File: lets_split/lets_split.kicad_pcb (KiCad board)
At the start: 2 copper layers, 112 x 79 mm, 62 parts, among them J1 3PIN, J2 6PIN, J3 3PIN, SW1 SW_PUSH, SW10 SW_PUSH, SW11 SW_PUSH, SW12 SW_PUSH, SW13 SW_PUSH, SW14 SW_PUSH, SW15 SW_PUSH, SW16 SW_PUSH, SW17 SW_PUSH, SW18 SW_PUSH, SW19 SW_PUSH, SW2 SW_PUSH, SW21 SW_PUSH, SW22 SW_PUSH, SW23 SW_PUSH, SW3 SW_PUSH, SW4 SW_PUSH, SW5 SW_PUSH, SW6 SW_PUSH, SW7 SW_PUSH, SW8 SW_PUSH, SW9 SW_PUSH, U2 HOLE, U3 HOLE, U4 HOLE, U5 HOLE

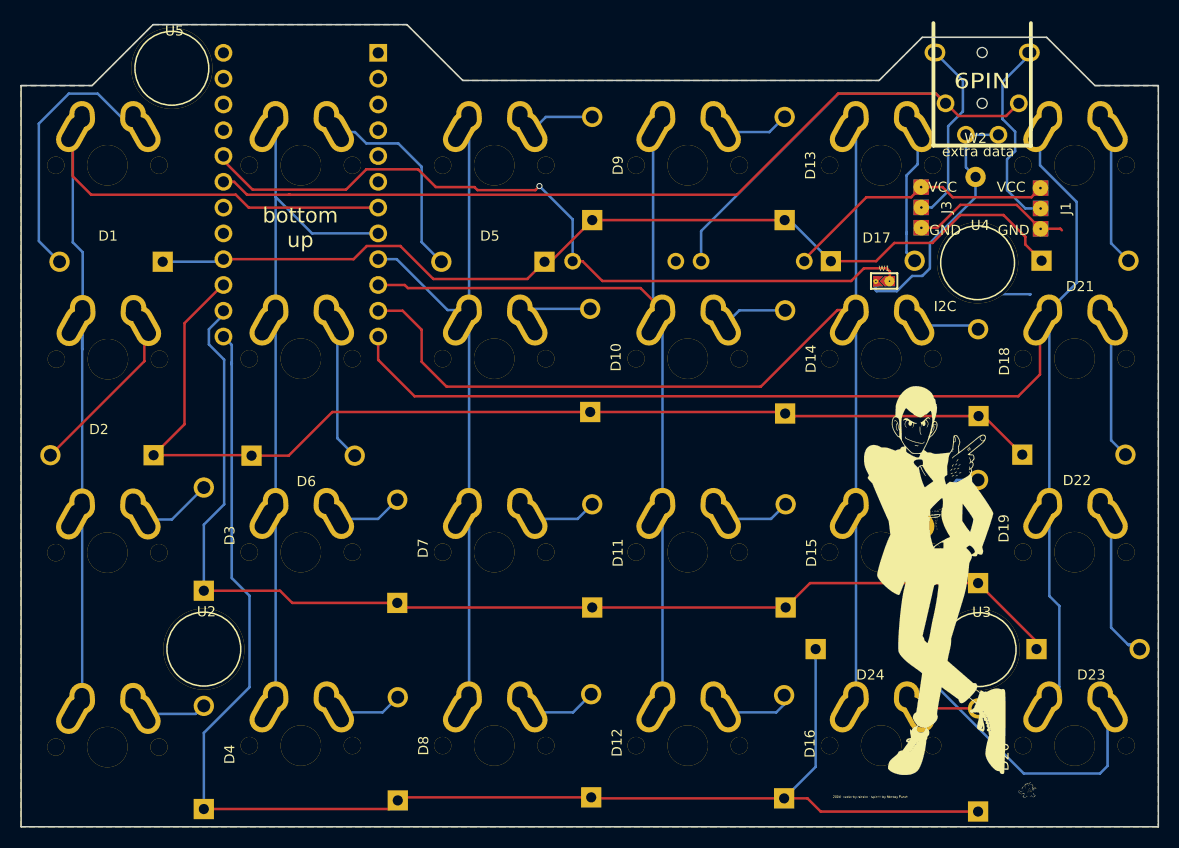
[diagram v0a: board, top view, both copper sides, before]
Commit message: Replace diode modules with SMD compatible one
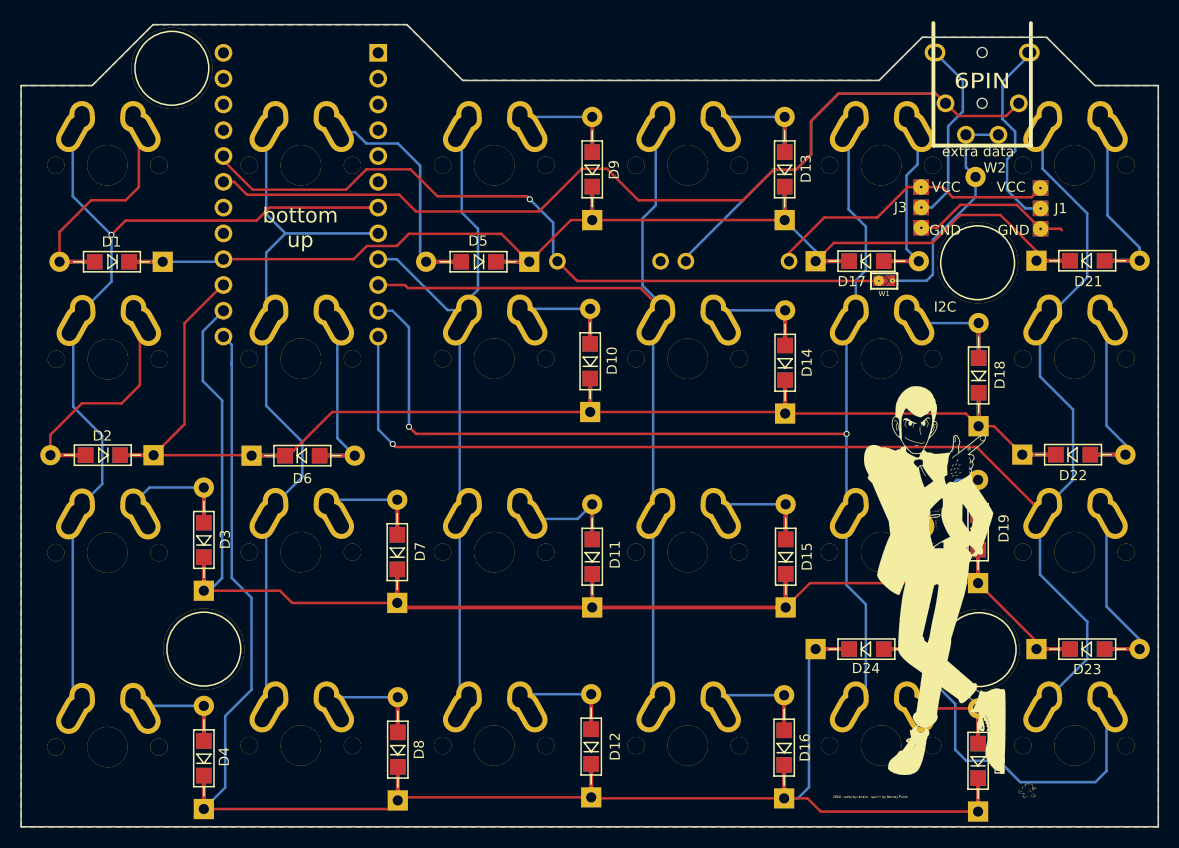
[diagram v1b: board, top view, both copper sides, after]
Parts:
- D1, D10, D11, D12, D13, D14, D15, D16, D17, D18, D19, D2, D20, D21, D22, D23, D24, D3, D4, D5, D6, D7, D8, D9: footprint Diodes_ThroughHole:Diode_DO-41_SOD81_Horizontal_RM10 -> local:Diode_TH_SOD123
- U1: value (none) -> TEENSY2.0
- moved D17 1.50 mm to (115.2, 56.3)
- moved D5 1.50 mm to (87.0, 56.4)
- moved R1 1.50 mm to (94.9, 56.3)
- moved R2 1.50 mm to (107.5, 56.3)
- moved D21 1.10 mm to (137.0, 56.2)
- moved D18 1.00 mm to (131.3, 72.5)
- turned W1 to 180 degrees
- gave numbers to parts that had none: 2
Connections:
- U1 pad 1: Net-(U1-Pad1) -> (no net)
- U1 pad 22: Net-(U1-Pad22) -> (no net)
- U1 pad 23: Net-(U1-Pad23) -> (no net)
- U1 pad 28: Net-(U1-Pad28) -> (no net)
- U1 pad 29: Net-(U1-Pad29) -> (no net)
- U1 pad 3: Net-(U1-Pad3) -> (no net)
- U1 pad 5: Net-(U1-Pad5) -> (no net)
- U1 pad 6: Net-(U1-Pad6) -> (no net)
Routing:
- net row3: track 143.1 -> 183.6 mm
- net row1: track 108.7 -> 148.7 mm
- net row2: track 117.3 -> 156.9 mm
- net row0: track 96.8 -> 136.2 mm
- net col0: track 96.5 -> 85.3 mm, vias 0 -> 1
- net Net-(D24-Pad2): track 30.5 -> 40.9 mm
- net Net-(D16-Pad2): track 7.14 -> 16.7 mm
- net Net-(D15-Pad2): track 6.65 -> 15.9 mm
- net Net-(D8-Pad2): track 6.57 -> 15.8 mm
- net Net-(D13-Pad2): track 6.57 -> 15.8 mm
- net Net-(D14-Pad2): track 6.62 -> 15.9 mm
- net Net-(D9-Pad2): track 6.67 -> 15.9 mm
- net Net-(D12-Pad2): track 6.69 -> 15.9 mm
- net Net-(D7-Pad2): track 6.69 -> 15.9 mm
- net Net-(D3-Pad2): track 7.20 -> 16.4 mm
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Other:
- net class Default: clearance 0.2 -> 0
- rule trace_clearance: 0.2 -> 0

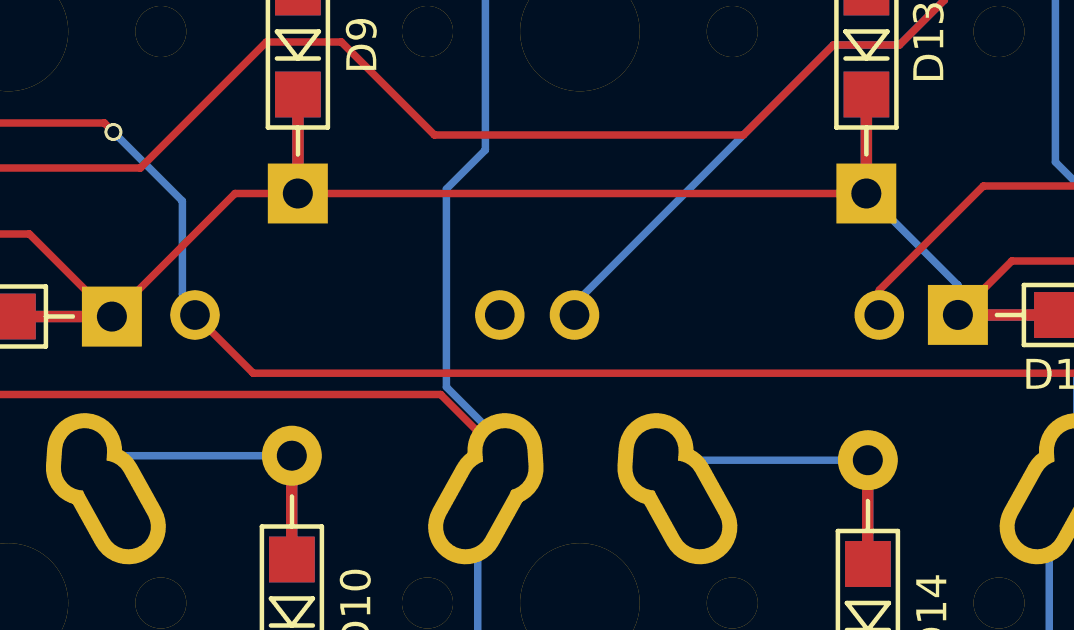
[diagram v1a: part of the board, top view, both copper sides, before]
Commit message: Replace resistor footprint with one having silk on both sides
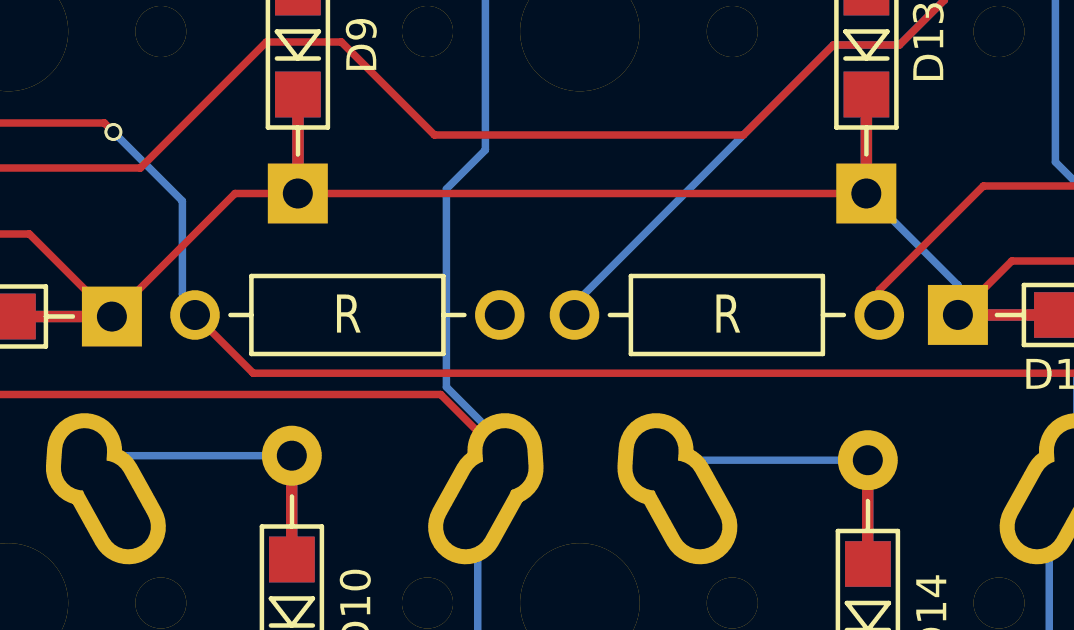
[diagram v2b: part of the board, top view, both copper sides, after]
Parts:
- R1, R2: footprint footprint:RESISTOR -> local:RESISTOR
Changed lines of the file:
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@@
     (add_net xtradata)
   )
+  (module local:RESISTOR (layer B.Cu)
+    (at 94.9 56.3 180)
+    (fp_text reference R1 (at 0 0 180) (layer B.SilkS) hide
+      (effects (font (size 1.27 1.016) (thickness 0.2032)) (justify mirror))
+    )
+    (fp_text value R (at 0 0) (layer B.SilkS)
+      (effects (font (size 1.27 1.016) (thickness 0.2032)) (justify mirror))
+    )
+    (fp_text user R (at 0 0 180) (layer F.SilkS)
+      (effects (font (size 1.27 1.016) (thickness 0.15)))
+    )
+    (fp_line (start 3.2 0) (end 3.9 0) (layer F.SilkS) (width 0.15))
+    (fp_line (start -3.2 -1.3) (end -3.2 1.3) (layer F.SilkS) (width 0.15))
+    (fp_line (start -3.2 1.3) (end 3.2 1.3) (layer F.SilkS) (width 0.15))
+    (fp_line (start 3.2 1.3) (end 3.2 -1.3) (layer F.SilkS) (width 0.15))
+    (fp_line (start 3.2 -1.3) (end -3.2 -1.3) (layer F.SilkS) (width 0.15))
+    (fp_line (start -3.9 0) (end -3.2 0) (layer F.SilkS) (width 0.15))
+    (fp_line (start 3.2 1.3) (end 3.2 -1.3) (layer B.SilkS) (width 0.15))
+    (fp_line (start 3.2 -1.3) (end -3.2 -1.3) (layer B.SilkS) (width 0.15))
+    (fp_line (start -3.2 -1.3) (end -3.2 1.3) (layer B.SilkS) (width 0.15))
+    (fp_line (start -3.2 1.3) (end 3.2 1.3) (layer B.SilkS) (width 0.15))
+    (fp_line (start -3.2 0) (end -3.9 0) (layer B.SilkS) (width 0.15))
+    (fp_line (start 3.2 0) (end 3.9 0) (layer B.SilkS) (width 0.15))
+    (fp_line (start -3.175 -1.27) (end -3.175 1.27) (layer Cmts.User) (width 0.381))
+    (fp_line (start 3.175 -1.27) (end -3.175 -1.27) (layer Cmts.User) (width 0.381))
+    (fp_line (start 3.175 1.27) (end 3.175 -1.27) (layer Cmts.User) (width 0.381))
+    (fp_line (start -3.175 1.27) (end 3.175 1.27) (layer Cmts.User) (width 0.381))
+    (fp_line (start 0 0) (end 0 0) (layer Dwgs.User) (width 0.0254))
+    (fp_line (start -3.175 -1.27) (end -3.175 1.27) (layer Dwgs.User) (width 0.381))
+    (fp_line (start 3.175 -1.27) (end -3.175 -1.27) (layer Dwgs.User) (width 0.381))
+    (fp_line (start 3.175 1.27) (end 3.175 -1.27) (layer Dwgs.User) (width 0.381))
+    (fp_line (start -3.175 1.27) (end 3.175 1.27) (layer Dwgs.User) (width 0.381))
+    (pad 2 thru_hole circle (at 5.08 0 180) (size 1.651 1.651) (drill 1) (layers *.Cu *.Mask)
+      (net 35 "Net-(R1-Pad2)"))
+    (pad 1 thru_hole circle (at -5.08 0 180) (size 1.651 1.651) (drill 1) (layers *.Cu *.Mask)
+      (net 31 VCC))
+  )
+  (module local:RESISTOR (layer B.Cu)
+    (at 107.55 56.3)
+    (fp_text reference R2 (at 0 0) (layer B.SilkS) hide
+      (effects (font (size 1.27 1.016) (thickness 0.2032)) (justify mirror))
+    )
+    (fp_text value R (at 0 0) (layer B.SilkS)
+      (effects (font (size 1.27 1.016) (thickness 0.2032)) (justify mirror))
+    )
+    (fp_text user R (at 0 0) (layer F.SilkS)
+      (effects (font (size 1.27 1.016) (thickness 0.15)))
+    )
+    (fp_line (start 3.2 0) (end 3.9 0) (layer F.SilkS) (width 0.15))
+    (fp_line (start -3.2 -1.3) (end -3.2 1.3) (layer F.SilkS) (width 0.15))
+    (fp_line (start -3.2 1.3) (end 3.2 1.3) (layer F.SilkS) (width 0.15))
+    (fp_line (start 3.2 1.3) (end 3.2 -1.3) (layer F.SilkS) (width 0.15))
+    (fp_line (start 3.2 -1.3) (end -3.2 -1.3) (layer F.SilkS) (width 0.15))
+    (fp_line (start -3.9 0) (end -3.2 0) (layer F.SilkS) (width 0.15))
+    (fp_line (start 3.2 1.3) (end 3.2 -1.3) (layer B.SilkS) (width 0.15))
+    (fp_line (start 3.2 -1.3) (end -3.2 -1.3) (layer B.SilkS) (width 0.15))
+    (fp_line (start -3.2 -1.3) (end -3.2 1.3) (layer B.SilkS) (width 0.15))
+    (fp_line (start -3.2 1.3) (end 3.2 1.3) (layer B.SilkS) (width 0.15))
+    (fp_line (start -3.2 0) (end -3.9 0) (layer B.SilkS) (width 0.15))
+    (fp_line (start 3.2 0) (end 3.9 0) (layer B.SilkS) (width 0.15))
+    (fp_line (start -3.175 -1.27) (end -3.175 1.27) (layer Cmts.User) (width 0.381))
+    (fp_line (start 3.175 -1.27) (end -3.175 -1.27) (layer Cmts.User) (width 0.381))
+    (fp_line (start 3.175 1.27) (end 3.175 -1.27) (layer Cmts.User) (width 0.381))
+    (fp_line (start -3.175 1.27) (end 3.175 1.27) (layer Cmts.User) (width 0.381))
+    (fp_line (start 0 0) (end 0 0) (layer Dwgs.User) (width 0.0254))
+    (fp_line (start -3.175 -1.27) (end -3.175 1.27) (layer Dwgs.User) (width 0.381))
+    (fp_line (start 3.175 -1.27) (end -3.175 -1.27) (layer Dwgs.User) (width 0.381))
+    (fp_line (start 3.175 1.27) (end 3.175 -1.27) (layer Dwgs.User) (width 0.381))
+    (fp_line (start -3.175 1.27) (end 3.175 1.27) (layer Dwgs.User) (width 0.381))
+    (pad 2 thru_hole circle (at 5.08 0) (size 1.651 1.651) (drill 1) (layers *.Cu *.Mask)
+      (net 31 VCC))
+    (pad 1 thru_hole circle (at -5.08 0) (size 1.651 1.651) (drill 1) (layers *.Cu *.Mask)
+      (net 32 data))
+  )
   (module local:Diode_TH_SOD123 (layer F.Cu)
     (at 50.95 56.35 180)
@@
     (pad HOLE np_thru_hole circle (at 7.8994 0 270) (size 0.9906 0.9906) (drill 0.9906) (layers *.Cu *.Mask F.SilkS))
   )
-  (module footprint:RESISTOR (layer B.Cu)
-    (at 94.9 56.3 180)
-    (fp_text reference R1 (at 0 0 180) (layer B.SilkS) hide
-      (effects (font (size 1.27 1.016) (thickness 0.2032)) (justify mirror))
-    )
-    (fp_text value R (at 0 0) (layer B.SilkS)
-      (effects (font (size 1.27 1.016) (thickness 0.2032)) (justify mirror))
-    )
-    (fp_line (start -3.175 1.27) (end 3.175 1.27) (layer Dwgs.User) (width 0.381))
-    (fp_line (start 3.175 1.27) (end 3.175 -1.27) (layer Dwgs.User) (width 0.381))
-    (fp_line (start 3.175 -1.27) (end -3.175 -1.27) (layer Dwgs.User) (width 0.381))
-    (fp_line (start -3.175 -1.27) (end -3.175 1.27) (layer Dwgs.User) (width 0.381))
-    (fp_line (start 0 0) (end 0 0) (layer Dwgs.User) (width 0.0254))
-    (fp_line (start -3.175 1.27) (end 3.175 1.27) (layer Cmts.User) (width 0.381))
-    (fp_line (start 3.175 1.27) (end 3.175 -1.27) (layer Cmts.User) (width 0.381))
-    (fp_line (start 3.175 -1.27) (end -3.175 -1.27) (layer Cmts.User) (width 0.381))
-    (fp_line (start -3.175 -1.27) (end -3.175 1.27) (layer Cmts.User) (width 0.381))
-    (fp_line (start -3.175 1.27) (end 3.175 1.27) (layer B.SilkS) (width 0.381))
-    (fp_line (start 3.175 1.27) (end 3.175 -1.27) (layer B.SilkS) (width 0.381))
-    (fp_line (start 3.175 -1.27) (end -3.175 -1.27) (layer B.SilkS) (width 0.381))
-    (fp_line (start -3.175 -1.27) (end -3.175 1.27) (layer B.SilkS) (width 0.381))
-    (fp_line (start 5.08 0) (end 3.175 0) (layer B.SilkS) (width 0.381))
-    (fp_line (start -5.08 0) (end -3.175 0) (layer B.SilkS) (width 0.381))
-    (pad 1 thru_hole circle (at -5.08 0 180) (size 1.651 1.651) (drill 0.9906) (layers *.Cu *.SilkS *.Mask)
-      (net 31 VCC))
-    (pad 2 thru_hole circle (at 5.08 0 180) (size 1.651 1.651) (drill 0.9906) (layers *.Cu *.SilkS *.Mask)
-      (net 35 "Net-(R1-Pad2)"))
-  )
-  (module footprint:RESISTOR (layer B.Cu)
-    (at 107.55 56.3)
-    (fp_text reference R2 (at 0 0) (layer B.SilkS) hide
-      (effects (font (size 1.27 1.016) (thickness 0.2032)) (justify mirror))
-    )
-    (fp_text value R (at 0 0) (layer B.SilkS)
-      (effects (font (size 1.27 1.016) (thickness 0.2032)) (justify mirror))
-    )
-    (fp_line (start -3.175 1.27) (end 3.175 1.27) (layer Dwgs.User) (width 0.381))
-    (fp_line (start 3.175 1.27) (end 3.175 -1.27) (layer Dwgs.User) (width 0.381))
-    (fp_line (start 3.175 -1.27) (end -3.175 -1.27) (layer Dwgs.User) (width 0.381))
-    (fp_line (start -3.175 -1.27) (end -3.175 1.27) (layer Dwgs.User) (width 0.381))
-    (fp_line (start 0 0) (end 0 0) (layer Dwgs.User) (width 0.0254))
-    (fp_line (start -3.175 1.27) (end 3.175 1.27) (layer Cmts.User) (width 0.381))
-    (fp_line (start 3.175 1.27) (end 3.175 -1.27) (layer Cmts.User) (width 0.381))
-    (fp_line (start 3.175 -1.27) (end -3.175 -1.27) (layer Cmts.User) (width 0.381))
-    (fp_line (start -3.175 -1.27) (end -3.175 1.27) (layer Cmts.User) (width 0.381))
-    (fp_line (start -3.175 1.27) (end 3.175 1.27) (layer B.SilkS) (width 0.381))
-    (fp_line (start 3.175 1.27) (end 3.175 -1.27) (layer B.SilkS) (width 0.381))
-    (fp_line (start 3.175 -1.27) (end -3.175 -1.27) (layer B.SilkS) (width 0.381))
-    (fp_line (start -3.175 -1.27) (end -3.175 1.27) (layer B.SilkS) (width 0.381))
-    (fp_line (start 5.08 0) (end 3.175 0) (layer B.SilkS) (width 0.381))
-    (fp_line (start -5.08 0) (end -3.175 0) (layer B.SilkS) (width 0.381))
-    (pad 1 thru_hole circle (at -5.08 0) (size 1.651 1.651) (drill 0.9906) (layers *.Cu *.SilkS *.Mask)
-      (net 32 data))
-    (pad 2 thru_hole circle (at 5.08 0) (size 1.651 1.651) (drill 0.9906) (layers *.Cu *.SilkS *.Mask)
-      (net 31 VCC))
-  )
   (module flipalps:MXALPS_FLIP (layer F.Cu)

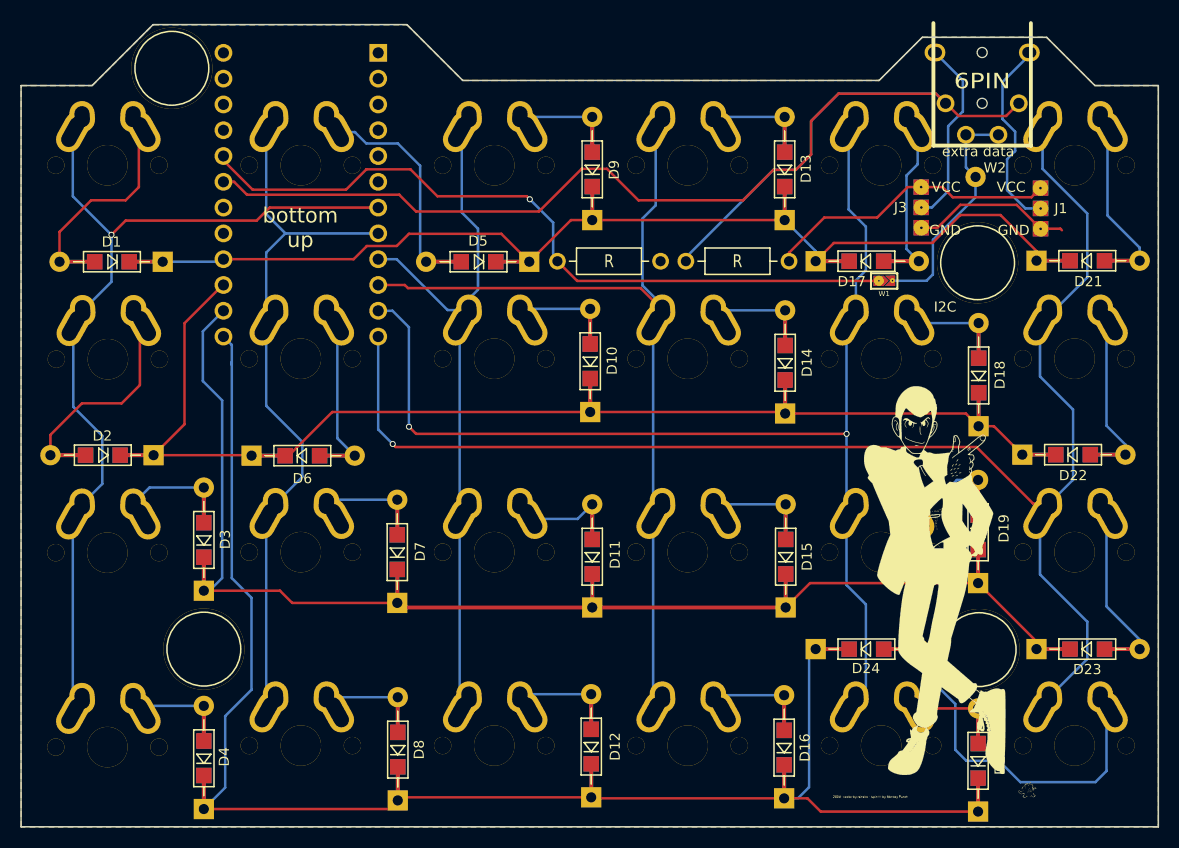
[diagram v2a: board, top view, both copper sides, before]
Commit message: Reorient horizontal diodes to match their direction
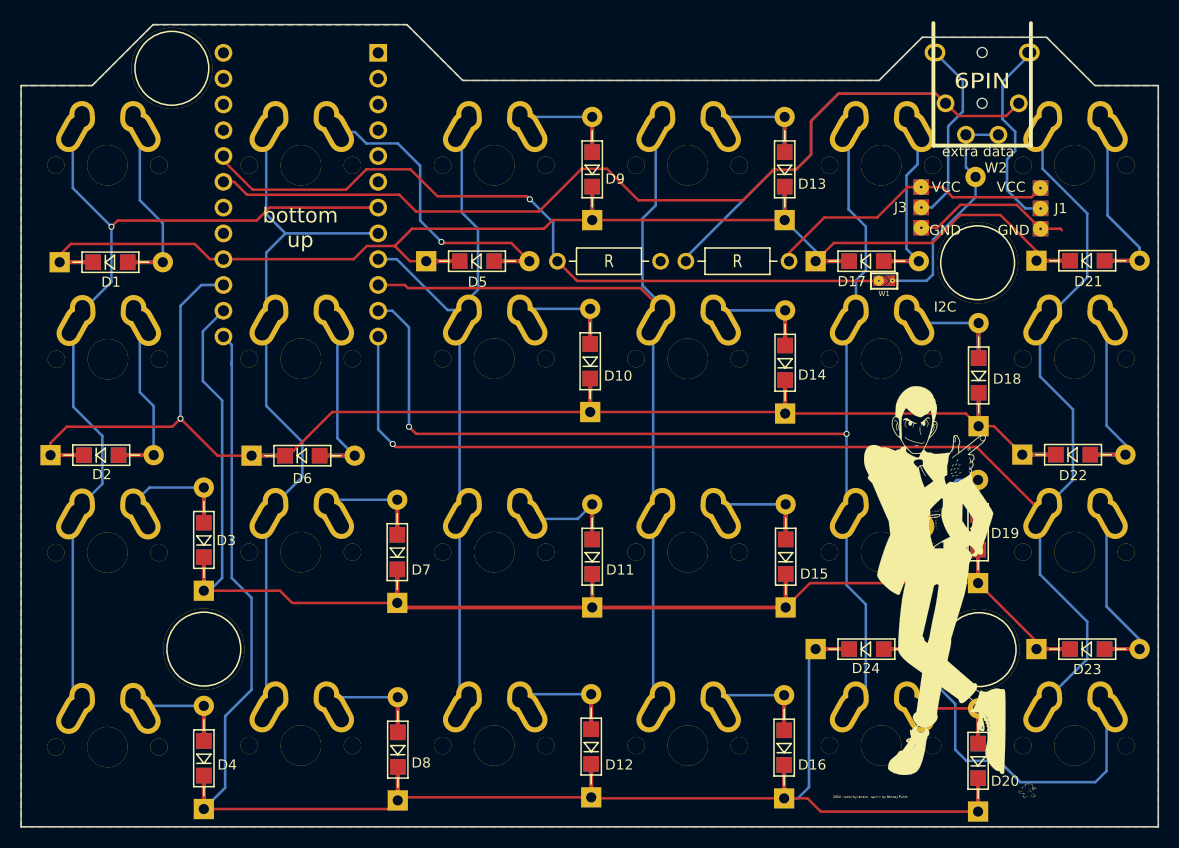
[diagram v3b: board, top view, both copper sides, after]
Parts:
- moved D1 10.2 mm to (40.8, 56.4), turned to 0 degrees
- moved D5 10.2 mm to (76.9, 56.3), turned to 0 degrees
- moved D2 10.1 mm to (39.9, 75.4), turned to 0 degrees
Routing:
- net row0: track 136.2 -> 149.5 mm
- net row1: track 148.7 -> 159.1 mm, vias 0 -> 1
- net Net-(D5-Pad2): track 26.1 -> 34.3 mm, vias 0 -> 1
- net Net-(D2-Pad2): track 25.8 -> 20.4 mm
- net Net-(D1-Pad2): track 25.1 -> 20.8 mm
